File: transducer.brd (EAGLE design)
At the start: 33 x 33 mm, 16 parts

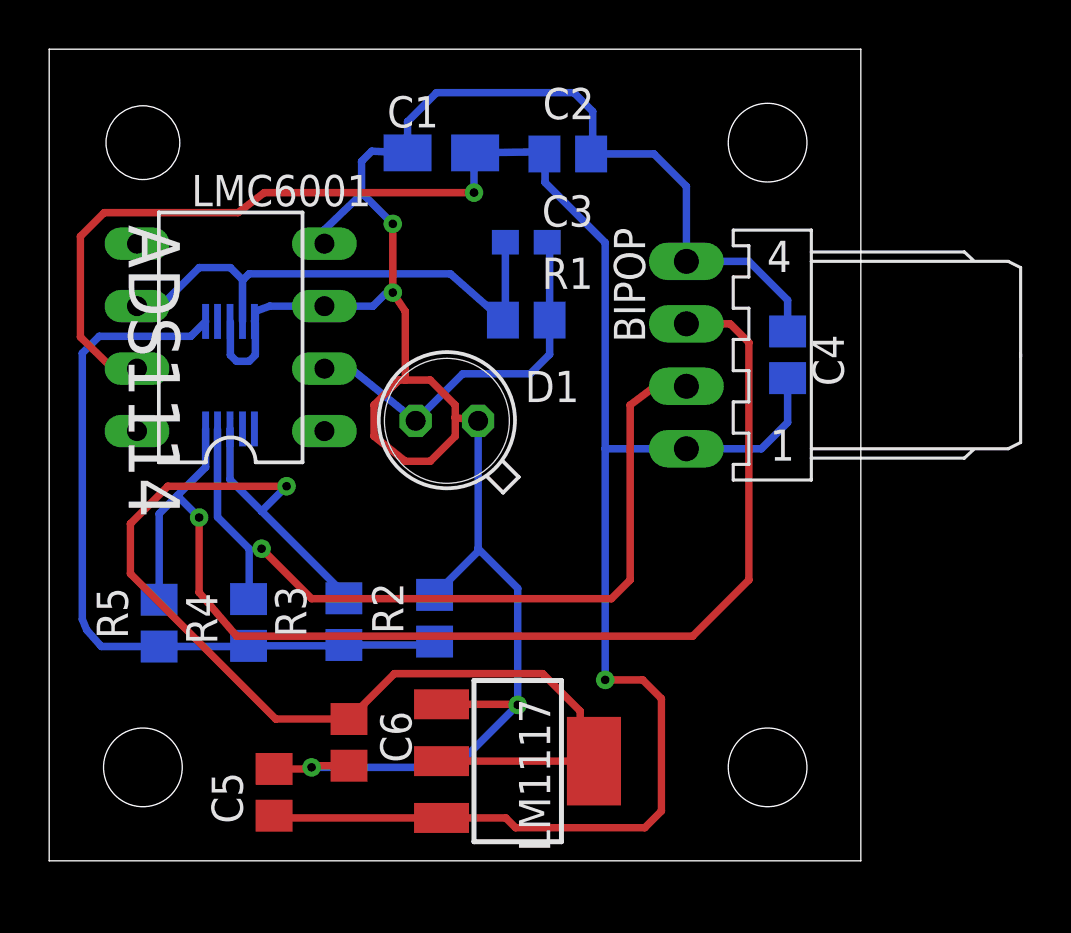
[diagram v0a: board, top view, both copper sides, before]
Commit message: transducer redesigned - alternative
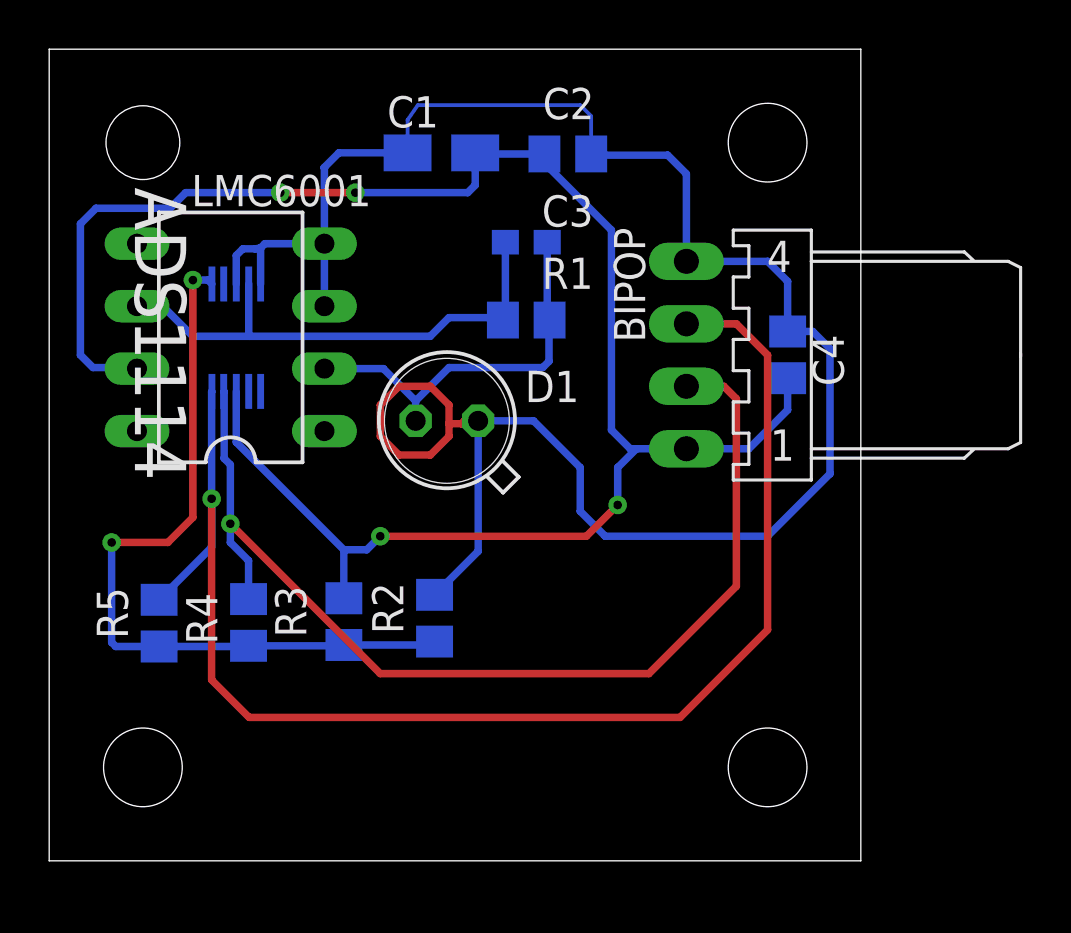
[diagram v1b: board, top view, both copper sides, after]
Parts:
- removed C5, C6: 100n, resistor:C0805
- removed LM1117: 3V3REGULATOR, 3v3lm1117:SOT223
- moved ADS1114 1.55 mm to (7.61, 68.3)
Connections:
- removed net 3.3V: ADS1114.8, C6.1, LM1117.2, LM1117.4, R3.2
- net 5V: now also ADS1114.8, R3.2; no longer C5.1, LM1117.3
- net GND: no longer C5.2, C6.2, LM1117.1
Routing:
- net 3.3V: track 49.9 -> 0.00 mm, vias 1 -> 0
- net SDA: track 33.8 -> 43.3 mm
- net 5V: track 83.7 -> 75.2 mm, vias 2 -> 4
- net GND: track 92.8 -> 84.6 mm, vias 4 -> 0
- net SCL: track 48.7 -> 56.4 mm
- net ADR: track 31.4 -> 31.6 mm, vias 0 -> 2

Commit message: SGlux version of transducer, new lib elements, transVIS deleted
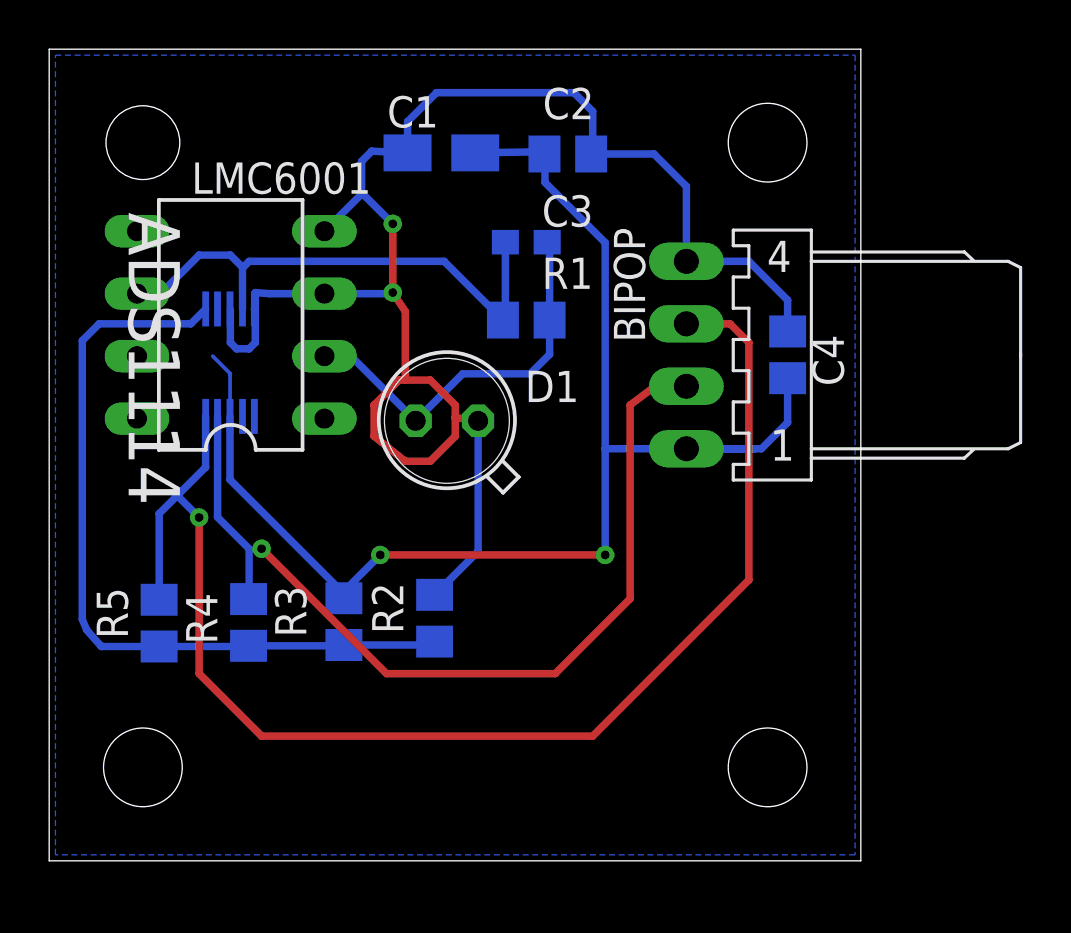
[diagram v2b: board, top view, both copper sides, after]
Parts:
- moved ADS1114 1.05 mm to (7.35, 67.3)
- moved LMC6001 0.51 mm to (7.38, 68.8)
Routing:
- net 5V: track 75.2 -> 55.9 mm, vias 4 -> 2
- net GND: track 84.6 -> 68.9 mm, vias 0 -> 2
- net SDA: track 43.3 -> 37.2 mm
- net SCL: track 56.4 -> 54.4 mm
- net U_OUT: track 21.1 -> 21.7 mm
- net ADR: track 31.6 -> 31.9 mm, vias 2 -> 0
- added copper zone on layer 16, net GND

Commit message: Transducer power supply and routing  modified.
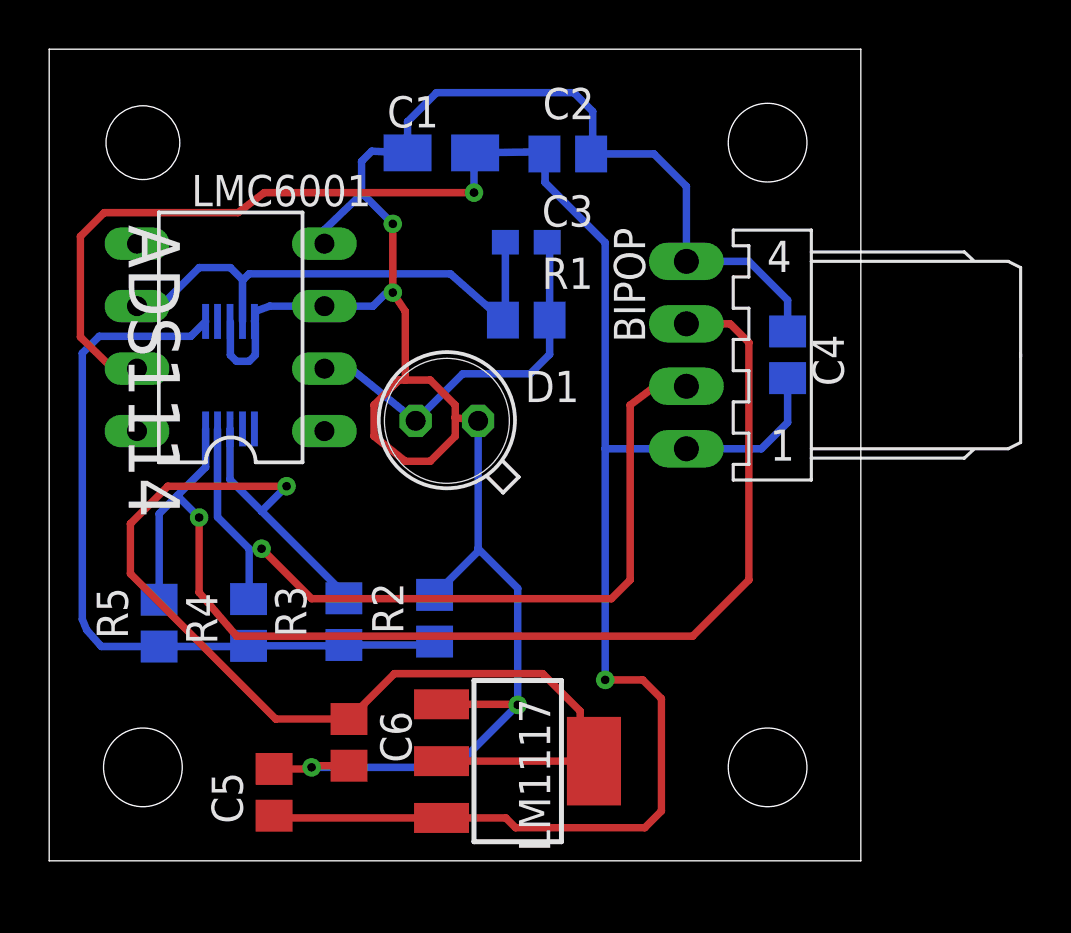
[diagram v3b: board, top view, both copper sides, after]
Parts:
- added C5, C6: 100n, resistor:C0805
- added LM1117: 3V3REGULATOR, 3v3lm1117:SOT223
- moved ADS1114 0.51 mm to (7.35, 66.7)
- moved LMC6001 0.51 mm to (7.38, 68.3)
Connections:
- new net 3.3V: ADS1114.8, C6.1, LM1117.2, LM1117.4, R3.2
- net 5V: now also C5.1, LM1117.3; no longer ADS1114.8, R3.2
- net GND: now also C5.2, C6.2, LM1117.1
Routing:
- net 3.3V: track 0.00 -> 49.9 mm, vias 0 -> 1
- net 5V: track 55.9 -> 83.7 mm
- net GND: track 68.9 -> 92.8 mm, vias 2 -> 4
- net SCL: track 54.4 -> 48.7 mm
- net SDA: track 37.2 -> 33.8 mm
- net ADR: track 31.9 -> 31.4 mm
- removed copper zone on layer 16, net GND
